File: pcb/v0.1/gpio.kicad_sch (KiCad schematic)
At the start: 0 parts

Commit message: Add co processor as its own sub page
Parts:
- added Module2: ComputeModule5-CM5, CM5IO:Raspberry-Pi-5-Compute-Module, symbol CM5IO:ComputeModule5-CM5
- added R2: 0R, Resistor_SMD:R_0603_1608Metric, symbol TH-1-CC:R_0Ω
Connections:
- new net +3.3v: R2.1
- new net GPIO_VREF: R2.2
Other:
- note added: "GPIO Voltage select"

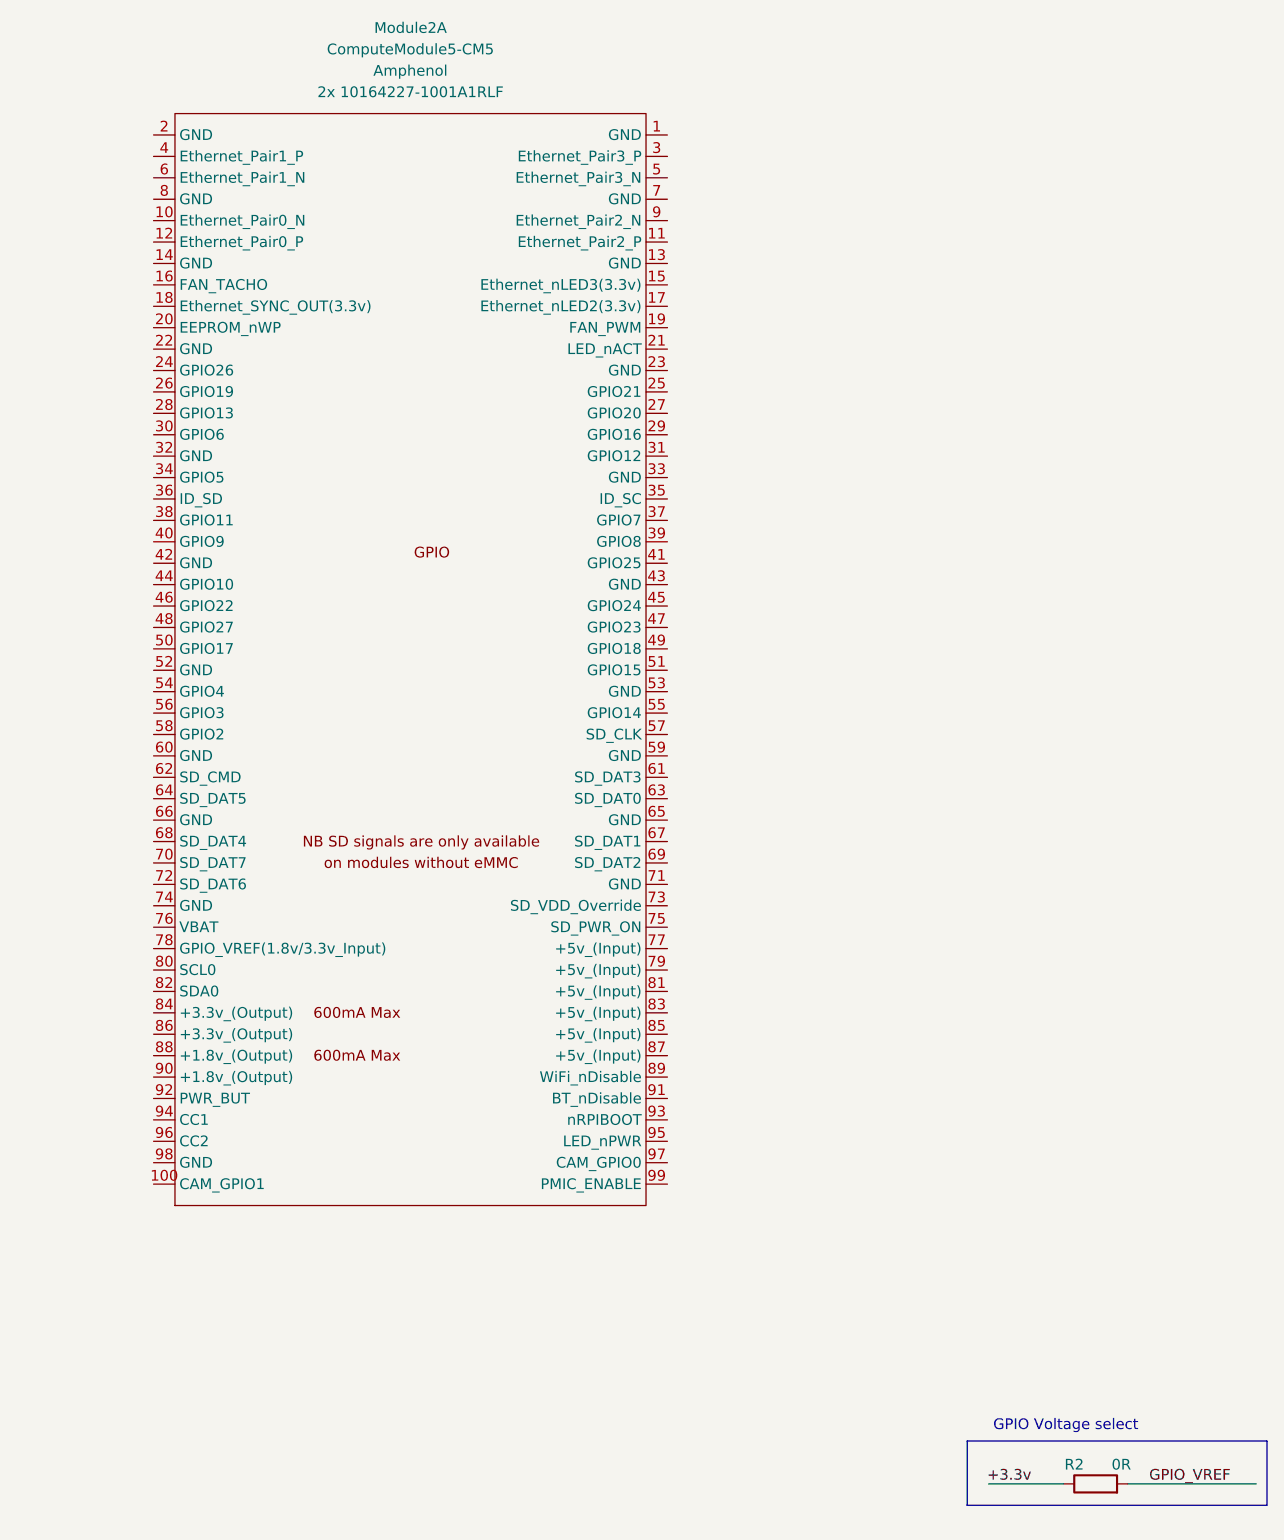
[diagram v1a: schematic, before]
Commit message: Add IR subsystem to schematic + clean up layout
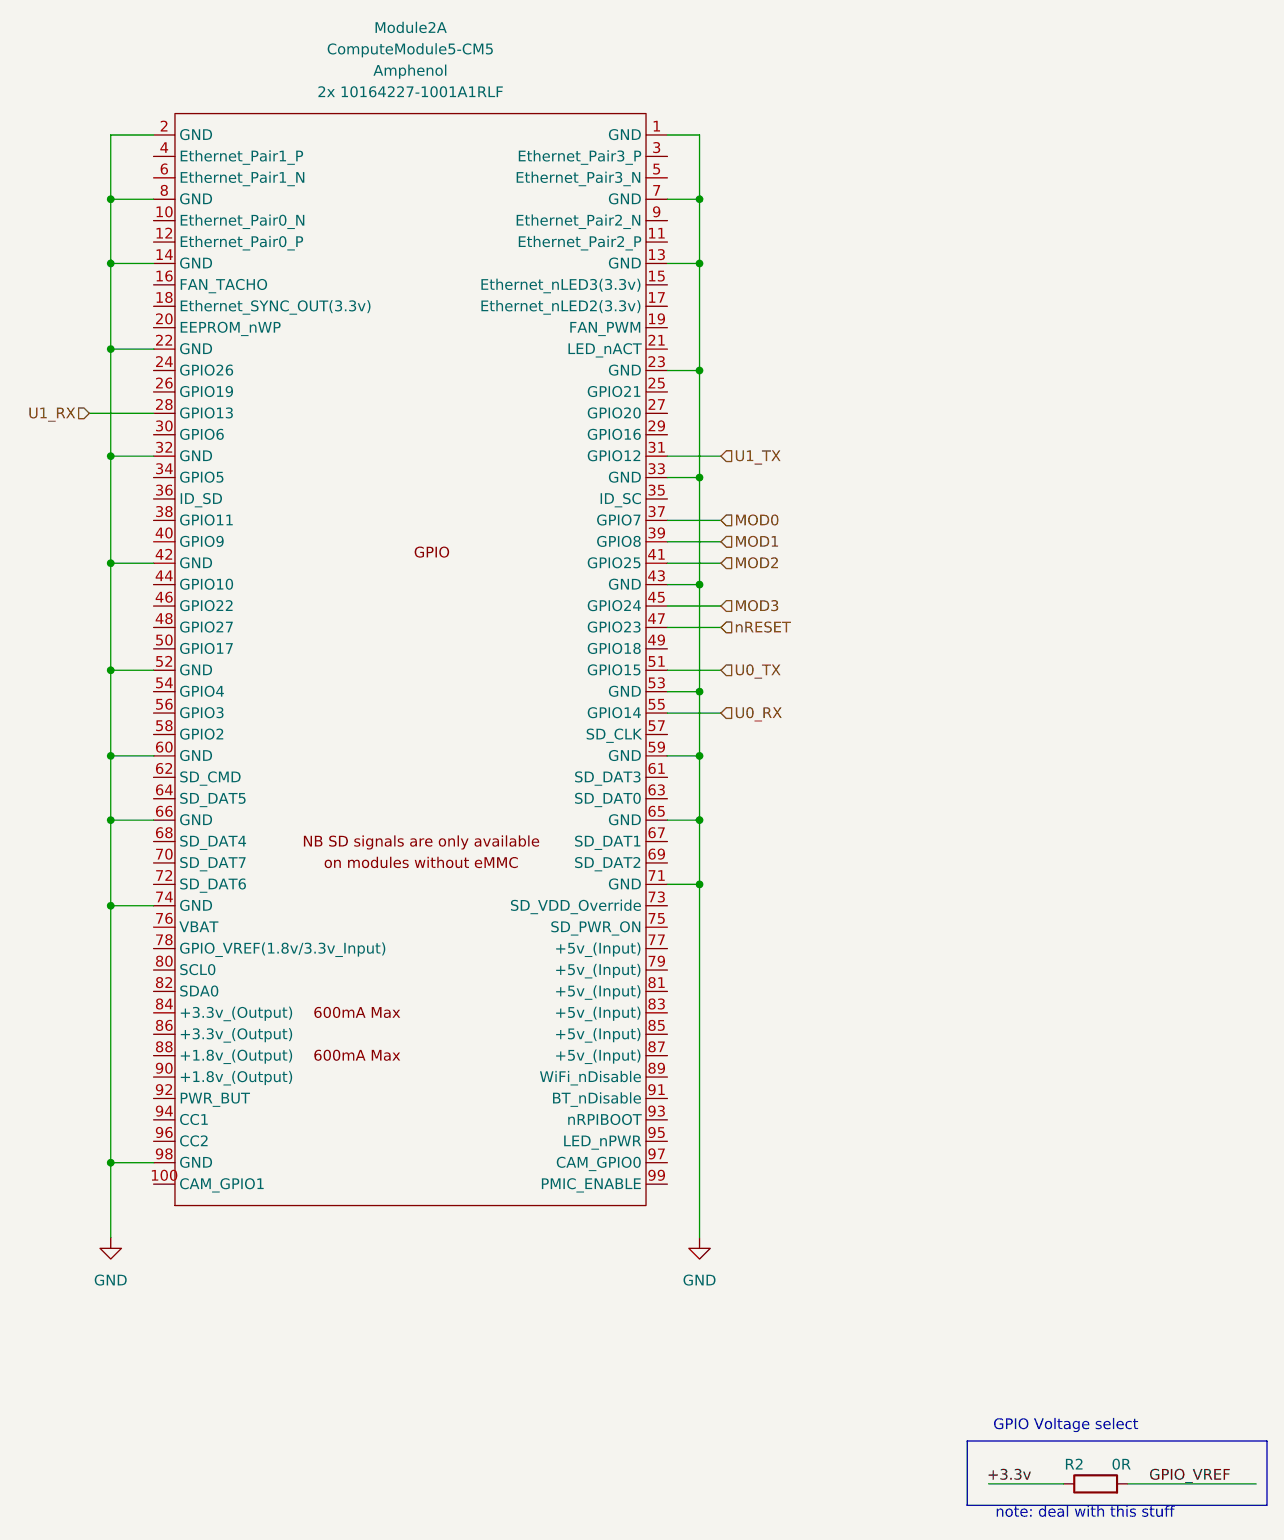
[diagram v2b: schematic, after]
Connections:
- net GND: now reaches Module2.1 (GND)
- net GND: now also Module2.13 (GND), Module2.14 (GND), Module2.2 (GND), Module2.22 (GND), Module2.23 (GND), Module2.32 (GND), Module2.33 (GND), Module2.42 (GND), Module2.43 (GND), Module2.52 (GND), Module2.53 (GND), Module2.59 (GND), Module2.60 (GND), Module2.65 (GND), Module2.66 (GND), Module2.7 (GND), Module2.71 (GND), Module2.74 (GND), Module2.8 (GND), Module2.98 (GND)
- net U1_RX: now reaches Module2.28 (GPIO13)
- net U1_TX: now reaches Module2.31 (GPIO12)
- net MOD0: now reaches Module2.37 (GPIO7)
- net MOD1: now reaches Module2.39 (GPIO8)
- net MOD2: now reaches Module2.41 (GPIO25)
- net MOD3: now reaches Module2.45 (GPIO24)
- net nRESET: now reaches Module2.47 (GPIO23)
- net U0_TX: now reaches Module2.51 (GPIO15)
- net U0_RX: now reaches Module2.55 (GPIO14)
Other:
- note added: "note: deal with this stuff"
- company: (none) -> Teahaz Computer
- title: (none) -> TH-1 Mainbaord devkit: GPIO

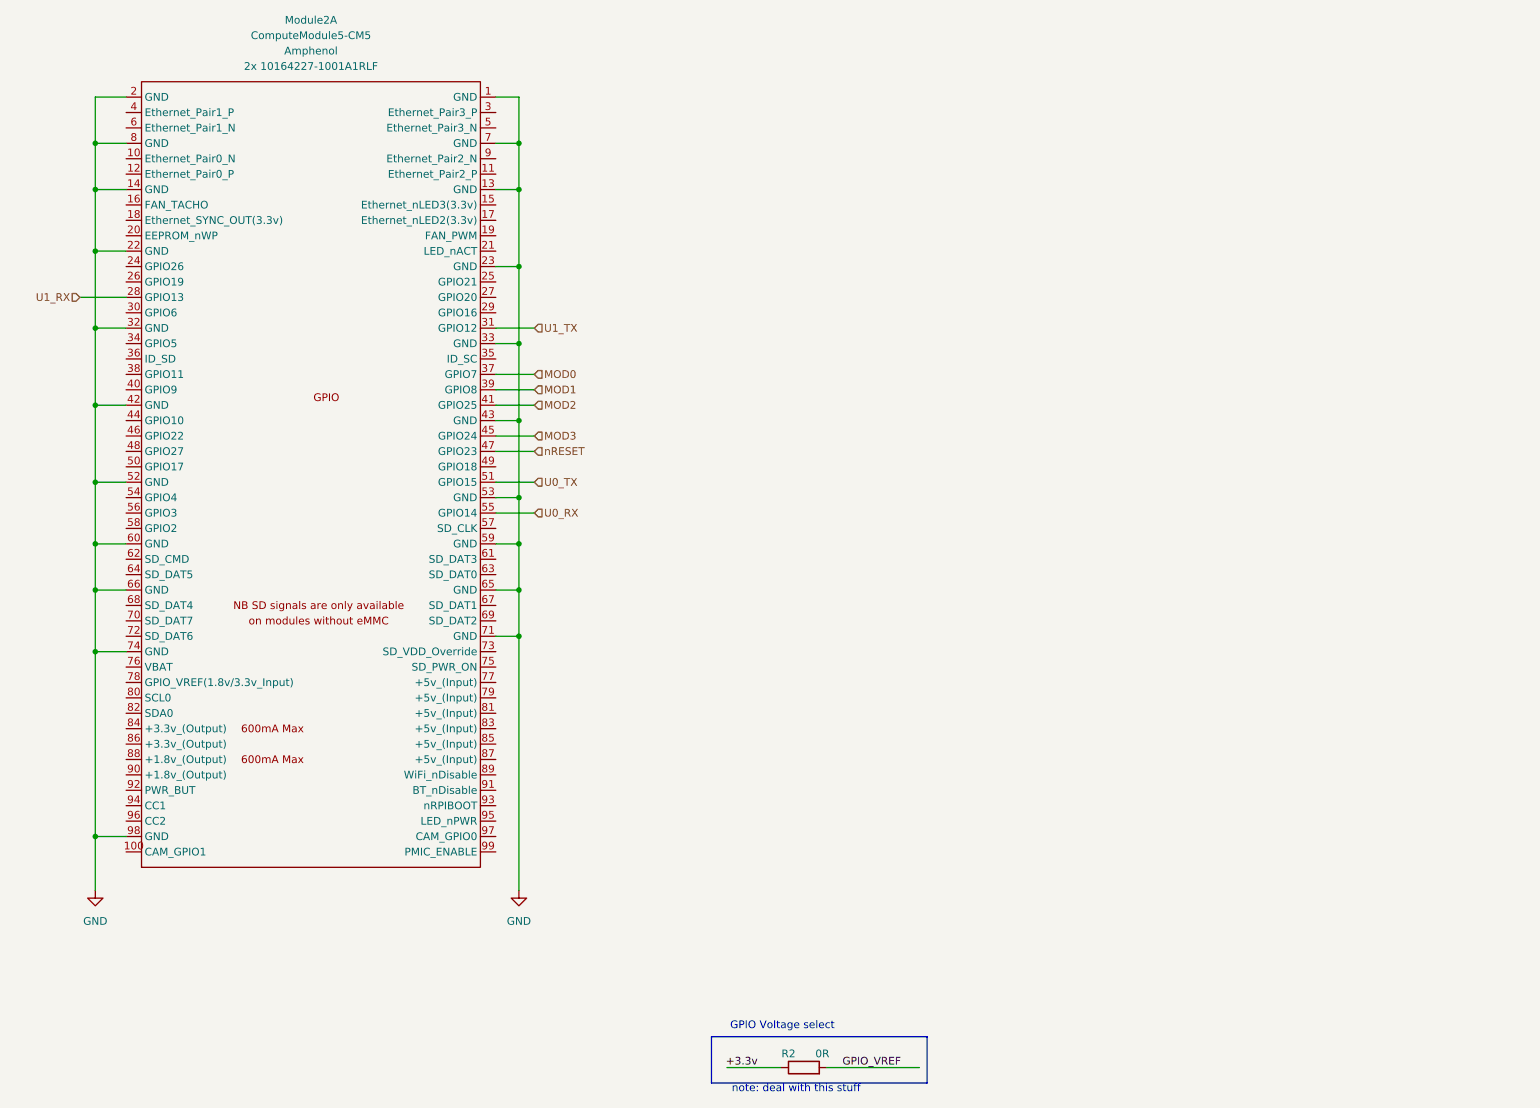
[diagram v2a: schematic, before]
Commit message: Continue mainboard schematic work
- Updated pins connecting to i2c and the co processor based on breadboard
testing.
- Added SD card reader
- Added power switch
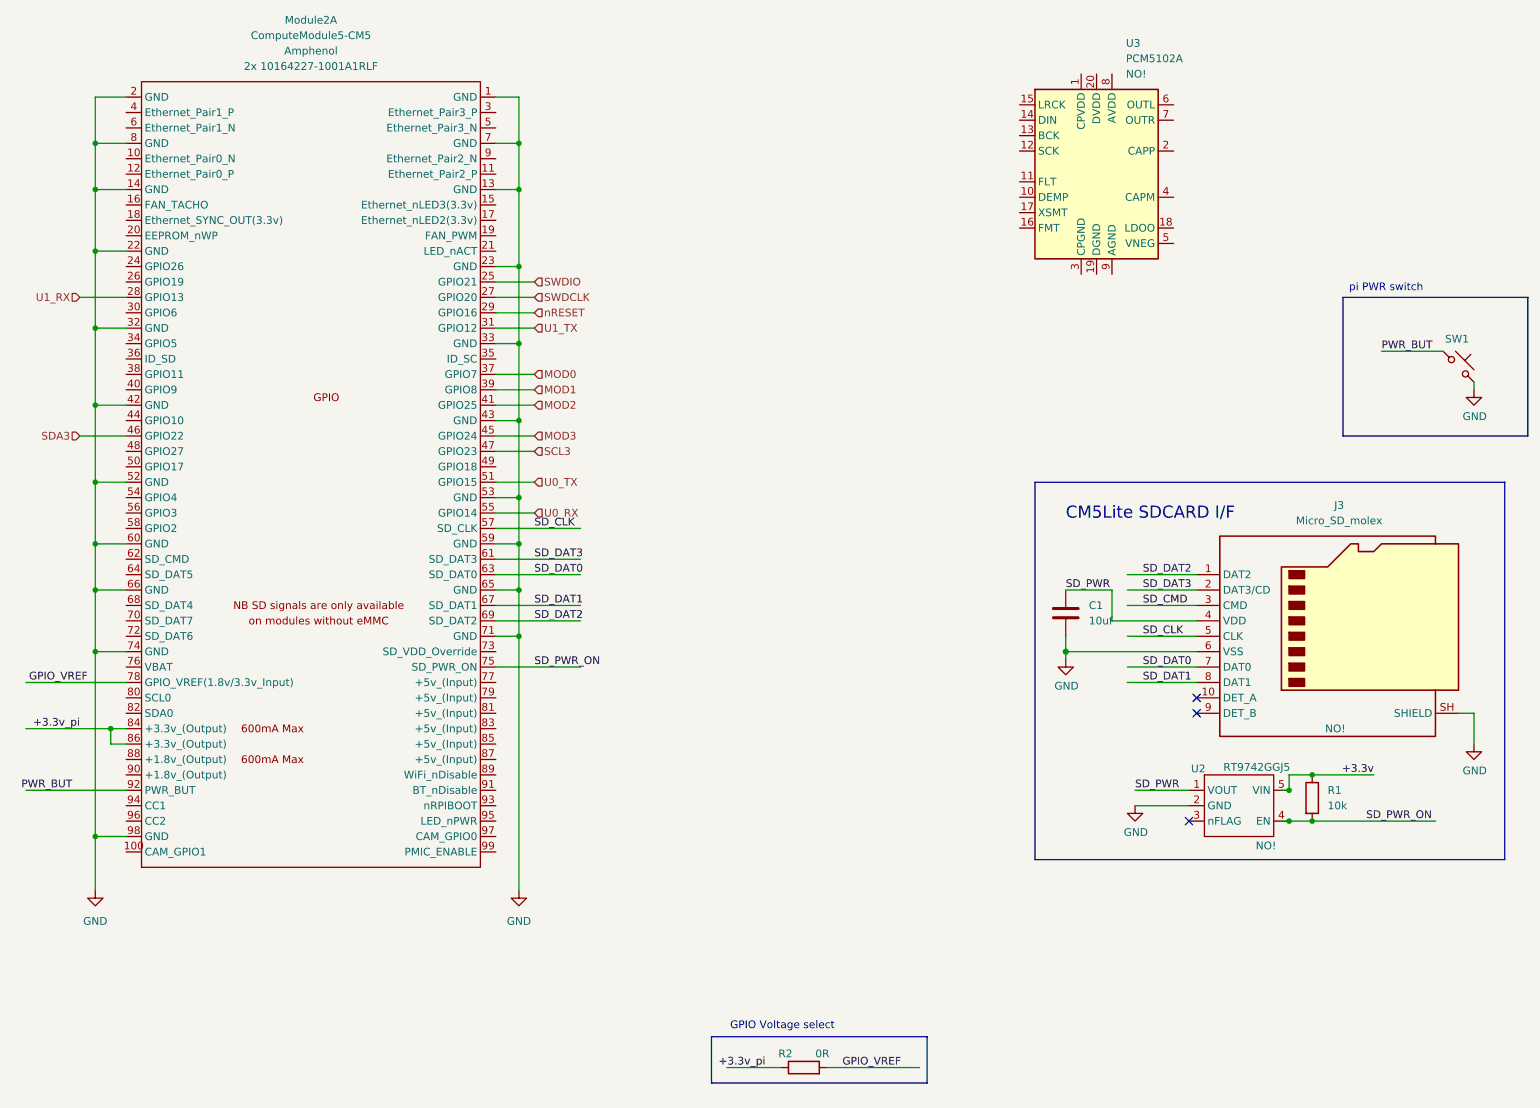
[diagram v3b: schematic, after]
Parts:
- added C1: 10uf, Capacitor_SMD:C_0805_2012Metric, symbol TH-1-CC:C_10uf
- added J3: Micro_SD_molex, symbol TH-1-CC:Micro_SD_molex
- added R1: 10k, Resistor_SMD:R_0603_1608Metric, symbol TH-1-CC:R_10k
- added SW1: SW_Push_45deg, symbol TH-1-CC:SW_Push_45deg
- added U2: RT9742GGJ5, Package_TO_SOT_SMD:TSOT-23-5, symbol TH-1-CC:RT9742GGJ5
- added U3: PCM5102A, Package_SO:TSSOP-20_4.4x6.5mm_P0.65mm, symbol TH-1-CC:PCM5102A
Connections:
- net +3.3v: now also R1.1, U2.5 (VIN); no longer R2.1
- net GND: now also C1.2, J3.6 (VSS), J3.SH (SHIELD), SW1.2, U2.2 (GND)
- net GPIO_VREF: now also Module2.78 (GPIO_VREF(1.8v/3.3v_Input))
- net nRESET: now also Module2.29 (GPIO16); no longer Module2.47 (GPIO23)
- net SWDIO: now reaches Module2.25 (GPIO21)
- net SWDCLK: now reaches Module2.27 (GPIO20)
- net SDA3: now reaches Module2.46 (GPIO22)
- net SD_CLK: now reaches Module2.57 (SD_CLK)
- net SD_CLK: now also J3.5 (CLK)
- net SD_DAT3: now reaches Module2.61 (SD_DAT3)
- net SD_DAT3: now also J3.2 (DAT3/CD)
- net SD_DAT0: now reaches Module2.63 (SD_DAT0)
- net SD_DAT0: now also J3.7 (DAT0)
- net SD_DAT1: now reaches Module2.67 (SD_DAT1)
- net SD_DAT1: now also J3.8 (DAT1)
- net SD_DAT2: now reaches Module2.69 (SD_DAT2)
- net SD_DAT2: now also J3.1 (DAT2)
- net SD_PWR_ON: now reaches Module2.75 (SD_PWR_ON)
- net SD_PWR_ON: now also R1.2, U2.4 (EN)
- net +3.3v_pi: now reaches Module2.84 (+3.3v_(Output))
- net +3.3v_pi: now also Module2.86 (+3.3v_(Output)), R2.1
- net PWR_BUT: now reaches Module2.92 (PWR_BUT)
- net PWR_BUT: now also SW1.1
- new net SCL3: Module2.47 (GPIO23)
- new net SD_CMD: J3.3 (CMD)
- new net SD_PWR: C1.1, J3.4 (VDD), U2.1 (VOUT)
- no-connect marks 0 -> 3
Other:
- note added: "CM5Lite SDCARD I/F"
- note added: "pi PWR switch"
- note removed: "note: deal with this stuff"

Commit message: More work on the sound system
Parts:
- added C15, C16, C18, C19: 10uf, Capacitor_SMD:C_0805_2012Metric, symbol TH-1-CC:C_10uf
- added C17: 100nf, Capacitor_SMD:C_0603_1608Metric, symbol TH-1-CC:C_100nf
- added C20: 2.2uf, Capacitor_SMD:C_0603_1608Metric, symbol TH-1-CC:C_2.2uf
- added FB1, FB2: FerriteBead_470, Resistor_SMD:R_0201_0603Metric, symbol TH-1-CC:FerriteBead_470
- added R2, R3, R4: 33Ω, Resistor_SMD:R_0603_1608Metric, symbol TH-1-CC:R_33Ω
- renumbered C1 to C7, J3 to J5, Module2 to Module1, R2 to R5, R1 to R6, U2 to U4
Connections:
- net +3.3v is gone; now on net +3.3v_pi: R6.1, U4.5 (VIN)
- net GND: now also U3.10 (DEMP), U3.11 (FLT), U3.12 (SCK), U3.16 (FMT), C15.1, C16.1, C17.2, C18.1, C19.1
- net DAC_A_VDD: now reaches U3.1 (CPVDD)
- net DAC_A_VDD: now also U3.8 (AVDD), C15.2, C16.2, C17.1, FB2.2
- net at U3.13 (BCK): now also R4.2
- net at U3.14 (DIN): now also R3.2
- net at U3.15 (LRCK): now also R2.2
- net at U3.18 (LDOO): now also C19.2
- net at U3.2 (CAPP): now also C20.1
- net DAC_D_VDD: now reaches U3.20 (DVDD)
- net DAC_D_VDD: now also C18.2, FB1.2
- net at U3.4 (CAPM): now also C20.2
- new net 3v3: FB1.1, FB2.1
- new net I2S_BCK: R4.1
- new net I2S_DIN: R3.1
- new net I2S_LRCK: R2.1
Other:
- moved on the sheet: C7, J5, R6, SW1, U3, U4

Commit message: Dac finished
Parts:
- added C12: 2.2uf, Capacitor_SMD:C_0603_1608Metric, symbol TH-1-CC:C_2.2uf
- added C14, C15: 2.2nf, Capacitor_SMD:C_0603_1608Metric, symbol TH-1-CC:C_2.2nf
- added C24: 100nf, Capacitor_SMD:C_0603_1608Metric, symbol TH-1-CC:C_100nf
- added R17: 10k, Resistor_SMD:R_0603_1608Metric, symbol TH-1-CC:R_10k
- added R18: 20k, Resistor_SMD:R_0603_1608Metric, symbol TH-1-CC:R_20k
- added R6, R7: 470Ω, Resistor_SMD:R_0603_1608Metric, symbol TH-1-CC:R_470Ω
- renumbered C17 to C10, C20 to C11, C19 to C13, C7 to C16, C18 to C7, C15 to C8, C16 to C9, R5 to R2, R2 to R3, R3 to R4, R4 to R5, R6 to R8
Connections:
- net GND: now also U3.19 (DGND), U3.3 (CPGND), U3.9 (AGND), C12.2, C14.2, C15.1, C24.2, R18.2
- net LDOO: now reaches C13.2, U3.18 (LDOO)
- net BCK: now reaches R5.2, U3.13 (BCK)
- net DIN: now reaches R4.2, U3.14 (DIN)
- net LRCK: now reaches R3.2, U3.15 (LRCK)
- net XSMT: now reaches U3.17 (XSMT)
- net XSMT: now also C24.1, R17.2, R18.1
- net CAPP: now reaches C11.1, U3.2 (CAPP)
- net CAPM: now reaches C11.2, U3.4 (CAPM)
- net VENG: now reaches U3.5 (VNEG)
- net VENG: now also C12.1
- net OUTL1: now reaches U3.6 (OUTL)
- net OUTL1: now also R6.1
- net OUTR1: now reaches U3.7 (OUTR)
- net OUTR1: now also R7.1
- new net 5v: R17.1
- new net OUTL: C14.1, R6.2
- new net OUTR: C15.2, R7.2
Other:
- note added: "Mute to avoid pops. Cap must fall to zero ~4ms before the regulator does."
- moved on the sheet: C16, J5, R2, R8, SW1, U4

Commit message: Add 3v3 regulator + reshuffle some connections.
Regulator ported over directly from PDB. I've also had to change around
some of the connections between modules to keep up with requirements.
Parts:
- added J7: AudioJack3, symbol TH-1-CC:AudioJack3
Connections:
- net GND: now also J7.S
- net OUTL: now also J7.T
- net OUTR: now also J7.R
- net USB2_CC1: now reaches Module1.94 (CC1)
- net USB2_CC2: now reaches Module1.96 (CC2)
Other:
- note added: "Audio subsystem"
- note added: "Note: Min impedence is 1k this port has no opamp and is only for speakers."
- moved on the sheet: C10, C11, C12, C13, C14, C15, C16, C24, C7, C8, C9, FB1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

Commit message: Clean up main page and power rails
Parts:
- added TP1: TestPoint, symbol Connector:TestPoint
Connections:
- net 5v is gone; now on net +5v: R17.1
- net I2S_BCK: now also Module1.49 (GPIO18)
- net I2S_DIN: now also Module1.25 (GPIO21)
- net I2S_LRCK: now also Module1.26 (GPIO19)
- net SWDIO: now also Module1.30 (GPIO6); no longer Module1.25 (GPIO21)
- net +5v: now reaches Module1.77 (+5v_(Input))
- net +5v: now also Module1.79 (+5v_(Input)), Module1.81 (+5v_(Input)), Module1.83 (+5v_(Input)), Module1.85 (+5v_(Input)), Module1.87 (+5v_(Input))
- net +3.3v_pi renamed +3v3_PI
- net 3v3 renamed +3v3_LDO
- net +3v3_LDO: now also TP1.1
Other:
- note added: "Add High side switch so its not powered when the pi is off. +10uf cap at switch out"
- moved on the sheet: C16, J5, R2, R8, SW1, U4
